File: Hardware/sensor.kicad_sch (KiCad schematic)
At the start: 12 parts, among them U1 OPA2376xxD

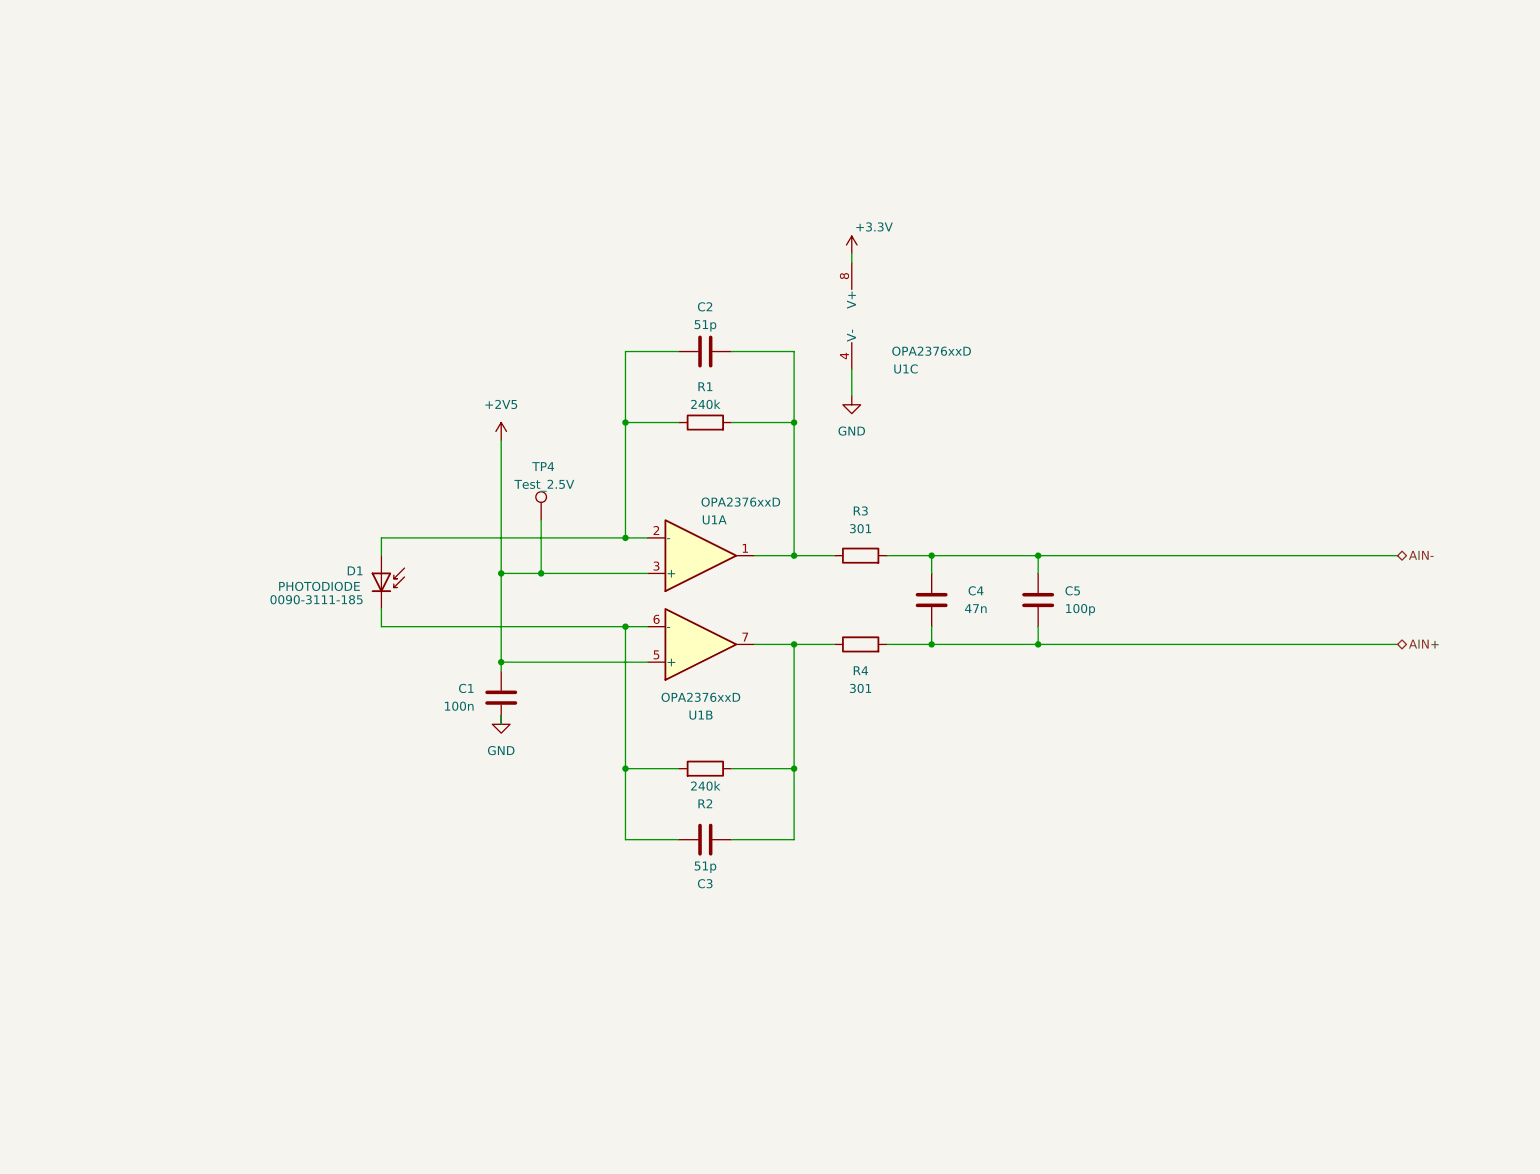
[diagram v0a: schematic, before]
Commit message: Version 0.6 - 4 layer version
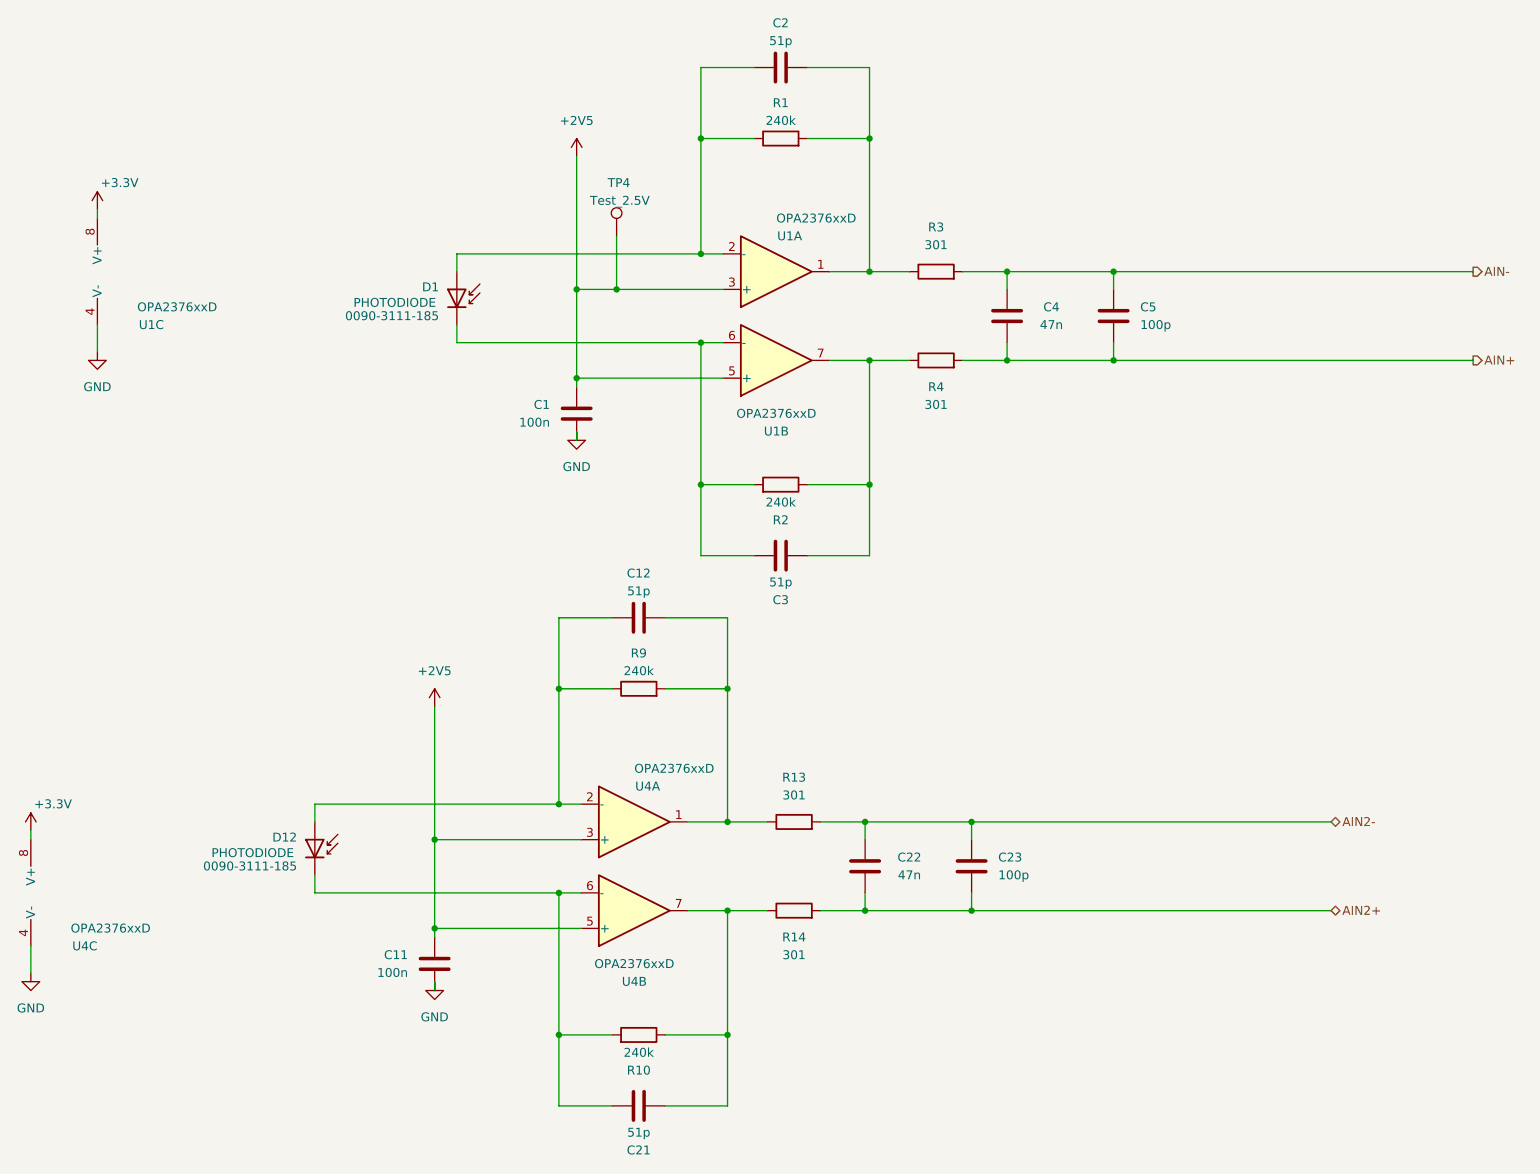
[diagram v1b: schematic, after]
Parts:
- added C11: 100n, Capacitor_SMD:C_0603_1608Metric_Pad1.08x0.95mm_HandSolder, symbol Device:C
- added C12, C21: 51p, Capacitor_SMD:C_0603_1608Metric_Pad1.08x0.95mm_HandSolder, symbol Device:C
- added C22: 47n, Capacitor_SMD:C_0603_1608Metric_Pad1.08x0.95mm_HandSolder, symbol Device:C
- added C23: 100p, Capacitor_SMD:C_0603_1608Metric_Pad1.08x0.95mm_HandSolder, symbol Device:C
- added D12: 0090-3111-185, Diode_SMD:D_1206_3216Metric_Pad1.42x1.75mm_HandSolder, symbol Device:D_Photo
- added R10, R9: 240k, Resistor_SMD:R_0603_1608Metric_Pad0.98x0.95mm_HandSolder, symbol Device:R
- added R13, R14: 301, Resistor_SMD:R_0603_1608Metric_Pad0.98x0.95mm_HandSolder, symbol Device:R
- added U4: OPA2376xxD, OPA2376AID:SOIC127P599X175-8N, symbol Amplifier_Operational:OPA2376xxD
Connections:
- net +2V5: now also C11.2, U4.3 (+), U4.5 (+)
- net +3V3: now also U4.8 (V+)
- net GND: now also C11.1, U4.4 (V-)
- new net: C12.2, R13.1, R9.2, U4.1
- new net: C12.1, D12.2 (A), R9.1, U4.2 (-)
- new net: C21.1, D12.1 (K), R10.2, U4.6 (-)
- new net: C21.2, R10.1, R14.1, U4.7
- new net AIN2+: C22.1, C23.2, R14.2
- new net AIN2-: C22.2, C23.1, R13.2
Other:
- moved on the sheet: C1, C2, C3, C4, C5, D1, R1, R2, R3, R4, TP4, U1A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
